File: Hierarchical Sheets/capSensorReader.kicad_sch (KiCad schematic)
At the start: 15 parts, among them U1 LM358, U2 LM358

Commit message: Redo Base Project file add code
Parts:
- removed V1, V2: 5, symbol Simulation_SPICE:VDC
- removed Vin1: VSIN, symbol Simulation_SPICE:VSIN
- C1: now left out of the parts list
- CSENSOR1: renamed from C2; now left out of the parts list
- Cf1, Cf2: footprint (none) -> Capacitor_THT:C_Disc_D3.8mm_W2.6mm_P2.50mm
- Ra1, Rb1, Rc1, Rd1, Rf1, Rf2: footprint (none) -> Resistor_THT:R_Axial_DIN0204_L3.6mm_D1.6mm_P5.08mm_Horizontal
- U2: footprint (none) -> Package_DIP:DIP-8_W7.62mm
- U2, U3: renamed from U1; footprint (none) -> Package_DIP:DIP-8_W7.62mm
- U3: renamed from U2; footprint (none) -> Package_DIP:DIP-8_W7.62mm
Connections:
- net V-: now reaches U2.4 (V-), U3.4 (V-)
- net Vsin: now reaches C1.1, CSENSOR1.1
- net V+: now reaches U2.8 (V+), U3.8 (V+)
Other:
- note removed: ".tran 10n 40u UIC"

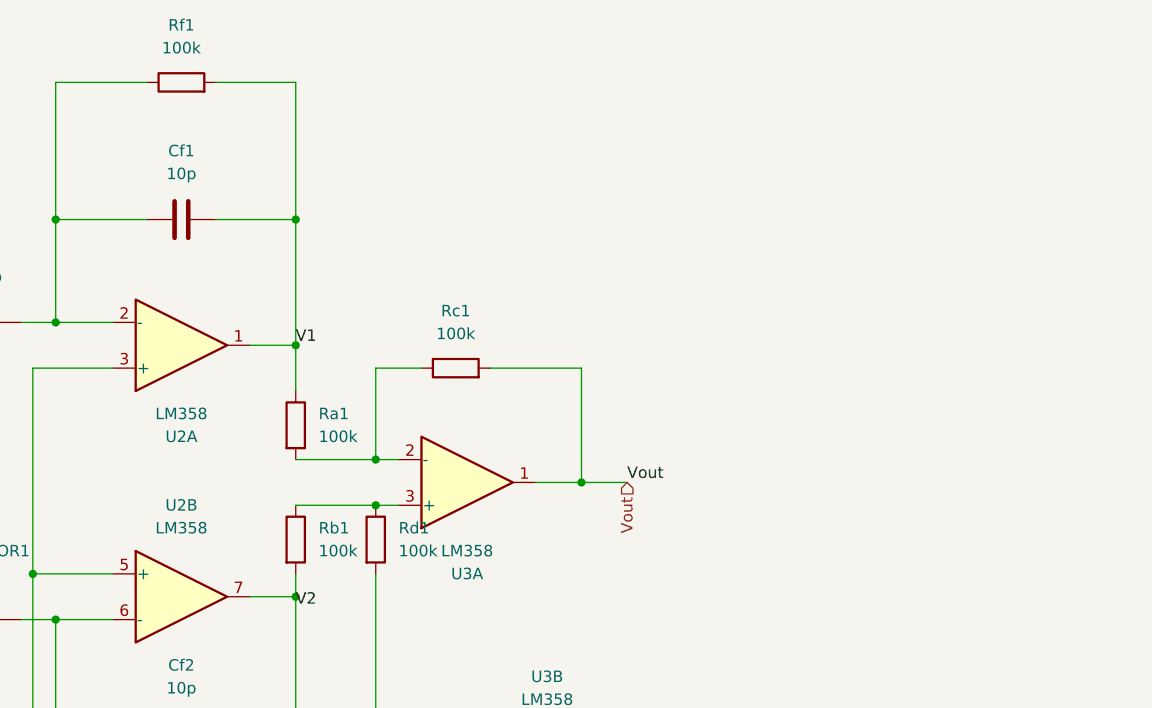
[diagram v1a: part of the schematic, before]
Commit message: Added rectifier and passive low-pass filter (RC)
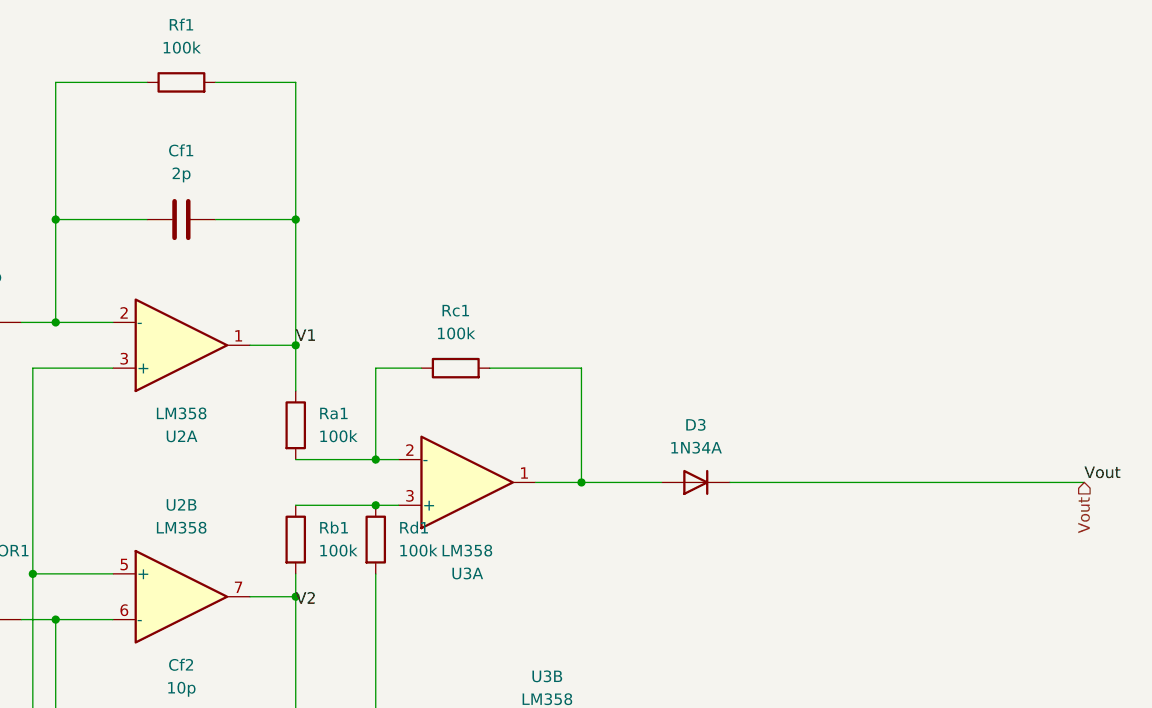
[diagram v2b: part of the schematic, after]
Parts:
- added D3: 1N34A, Diode_THT:D_DO-35_SOD27_P2.54mm_Vertical_AnodeUp, symbol Device:D
- Cf1: value 10p -> 2p
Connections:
- net Vout: now also D3.1 (K); no longer Rc1.2, U3.1
- new net: D3.2 (A), Rc1.2, U3.1
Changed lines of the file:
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@@
+	)
+	(junction
+		(at 114.3 59.69)
+		(diameter 0)
+		(color 0 0 0 0)
+	)
+	(junction
+		(at 111.76 99.06)
+		(diameter 0)
+		(color 0 0 0 0)
+	)
+	(junction
+		(at 149.86 91.44)
+		(diameter 0)
+		(color 0 0 0 0)
+	)
+	(junction
+		(at 140.97 101.6)
+		(diameter 0)
+		(color 0 0 0 0)
+	)
+	(junction
+		(at 114.3 104.14)
+		(diameter 0)
+		(color 0 0 0 0)
+	)
+	(junction
+		(at 140.97 59.69)
+		(diameter 0)
+		(color 0 0 0 0)
+	)
+	(junction
+		(at 114.3 71.12)
+		(diameter 0)
+		(color 0 0 0 0)
+	)
+	(junction
+		(at 140.97 116.84)
+		(diameter 0)
+		(color 0 0 0 0)
+	)
+	(junction
+		(at 66.04 100.33)
+		(diameter 0)
+		(color 0 0 0 0)
 	)
 	(junction
@@
 		(color 0 0 0 0)
 	)
-	(junction
-		(at 114.3 59.69)
-		(diameter 0)
-		(color 0 0 0 0)
-	)
-	(junction
-		(at 111.76 99.06)
-		(diameter 0)
-		(color 0 0 0 0)
-	)
-	(junction
-		(at 149.86 91.44)
-		(diameter 0)
-		(color 0 0 0 0)
-	)
-	(junction
-		(at 140.97 101.6)
-		(diameter 0)
-		(color 0 0 0 0)
-	)
-	(junction
-		(at 114.3 104.14)
-		(diameter 0)
-		(color 0 0 0 0)
-	)
-	(junction
-		(at 140.97 59.69)
-		(diameter 0)
-		(color 0 0 0 0)
-	)
-	(junction
-		(at 114.3 71.12)
-		(diameter 0)
-		(color 0 0 0 0)
-	)
-	(junction
-		(at 140.97 116.84)
-		(diameter 0)
-		(color 0 0 0 0)
-	)
-	(junction
-		(at 66.04 100.33)
-		(diameter 0)
-		(color 0 0 0 0)
-	)
 	(no_connect
 		(at 161.29 118.11)
@@
 	(wire
 		(pts
-			(xy 172.72 88.9) (xy 177.8 88.9)
-		)
-		(stroke
-			(width 0)
-			(type default)
-		)
-	)
-	(wire
-		(pts
 			(xy 135.89 73.66) (xy 140.97 73.66)
 		)
@@
 		(pts
 			(xy 132.08 44.45) (xy 140.97 44.45)
+		)
+		(stroke
+			(width 0)
+			(type default)
+		)
+	)
+	(wire
+		(pts
+			(xy 172.72 88.9) (xy 181.61 88.9)
+		)
+		(stroke
+			(width 0)
+			(type default)
+		)
+	)
+	(wire
+		(pts
+			(xy 189.23 88.9) (xy 228.6 88.9)
 		)
 		(stroke
@@
 	)
 	(label "Vout"
-		(at 177.8 88.9 0)
+		(at 228.6 88.9 0)
 		(effects
 			(font
@@
 	(hierarchical_label "Vout"
 		(shape input)
-		(at 177.8 88.9 270)
+		(at 228.6 88.9 270)
 		(effects
 			(font
@@
 			)
 		)
-		(property "Value" "10p"
+		(property "Value" "2p"
 			(at 128.27 54.61 90)
 			(effects
@@
 					(unit 1)
 				)
+			)
+		)
+	)
+	(symbol
+		(lib_id "Device:D")
+		(at 185.42 88.9 180)
+		(unit 1)
+		(exclude_from_sim no)
+		(in_bom yes)
+		(on_board yes)
+		(dnp no)
+		(fields_autoplaced yes)
+		(property "Reference" "D3"
+			(at 185.42 82.55 0)
+			(effects
+				(font
+					(size 1.27 1.27)
+				)
+			)
+		)
+		(property "Value" "1N34A"
+			(at 185.42 85.09 0)
+			(effects
+				(font
+					(size 1.27 1.27)
+				)
+			)
+		)
+		(property "Footprint" "Diode_THT:D_DO-35_SOD27_P2.54mm_Vertical_AnodeUp"
+			(at 185.42 88.9 0)
+			(effects
+				(font
+					(size 1.27 1.27)
+				)
+				(hide yes)
+			)
+		)
+		(property "Datasheet" "~"
+			(at 185.42 88.9 0)
+			(effects
+				(font
+					(size 1.27 1.27)
+				)
+				(hide yes)
+			)
+		)
+		(property "Description" "Diode"
+			(at 185.42 88.9 0)
+			(effects
+				(font
+					(size 1.27 1.27)
+				)
+				(hide yes)
+			)
+		)
+		(property "Sim.Library" ".\\"
+			(at 185.42 88.9 0)
+			(effects
+				(font
+					(size 1.27 1.27)
+				)
+				(hide yes)
+			)
+		)
+		(pin "1"
+		)
+		(pin "2"
+		)
+		(instances
+			(project ""
+				(path "/eb20fb8b-6e33-462b-9505-401dab49dd09/b20763cf-135f-4c80-a439-1f71268d237b"
+					(reference "D3")
+					(unit 1)
+				)
+				(path "/eb20fb8b-6e33-462b-9505-401dab49dd09/d1fc981b-0a3d-4bee-b8f0-81f28e3ff9d1"
+					(reference "D4")
+					(unit 1)
+				)

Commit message: Update Main Sub Sheets
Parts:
- removed Ra1, Rb1, Rd1: 100k, Resistor_THT:R_Axial_DIN0204_L3.6mm_D1.6mm_P5.08mm_Horizontal, symbol Device:R
- removed unit 1 of U3
- added C1, C13, C14: 100p, symbol Device:C
- added R11, Rc3, Rc5: 1k, symbol Device:R
- added R12: 500, symbol Device:R
- added Rc4: 100k, symbol Device:R
- added U3: INA128, symbol Amplifier_Instrumentation:INA128
- Rc1: footprint Resistor_THT:R_Axial_DIN0204_L3.6mm_D1.6mm_P5.08mm_Horizontal -> (none)
- renumbered C1 to C2, CSENSOR1 to CSENSOR2, Cf1 to Cf3, Cf2 to Cf4, Rf1 to Rf3, Rf2 to Rf4, U2 to U4, U3 to U5
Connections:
- net GND: now also C1.2, C13.2, C14.2, U3.5 (Ref)
- net V+: now also U3.7 (V+)
- net V-: now also U3.4 (V-)
- net V1: now also U3.3 (+)
- net V2: now also U3.2 (-)
- net Vout: now also U5.7, R11.2; no longer D3.1 (K)
- net at Rc1.1: now also D3.1 (K), C1.1
- net at Rc1.2: now also Rc3.2, Rc4.1; no longer D3.2 (A)
- net at U5.5 (+): now also Rc4.2, Rc5.2
- net at U5.6 (-): now also R11.1
- new net: C14.1, Rc5.1
- new net: R12.1, U3.1 (Rg)
- new net: D3.2 (A), U3.6
- new net: R12.2, U3.8 (Rg)
- new net: C13.1, Rc3.1
- no-connect marks 3 -> 0
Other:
- moved on the sheet: C2, CSENSOR2, Cf3, Cf4, Rf3, Rf4, U4A, U4B, U5B

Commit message: Main Update
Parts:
- C16: renamed from C1; footprint (none) -> Capacitor_THT:C_Disc_D3.8mm_W2.6mm_P2.50mm
- C17: renamed from C13; footprint (none) -> Capacitor_THT:C_Disc_D3.8mm_W2.6mm_P2.50mm
- C18: renamed from C14; footprint (none) -> Capacitor_THT:C_Disc_D3.8mm_W2.6mm_P2.50mm
- R13: renamed from R12; footprint (none) -> Resistor_THT:R_Axial_DIN0204_L3.6mm_D1.6mm_P5.08mm_Horizontal
- R14: renamed from R11; footprint (none) -> Resistor_THT:R_Axial_DIN0204_L3.6mm_D1.6mm_P5.08mm_Horizontal
- Rc2: renamed from Rc1; footprint (none) -> Resistor_THT:R_Axial_DIN0204_L3.6mm_D1.6mm_P5.08mm_Horizontal
- Rc6: renamed from Rc3; footprint (none) -> Resistor_THT:R_Axial_DIN0204_L3.6mm_D1.6mm_P5.08mm_Horizontal
- Rc7: renamed from Rc4; footprint (none) -> Resistor_THT:R_Axial_DIN0204_L3.6mm_D1.6mm_P5.08mm_Horizontal
- Rc8: renamed from Rc5; footprint (none) -> Resistor_THT:R_Axial_DIN0204_L3.6mm_D1.6mm_P5.08mm_Horizontal
- U13: renamed from U3; footprint (none) -> Package_DIP:DIP-8_W7.62mm
- renumbered C2 to C15, CSENSOR2 to CSENSOR1, Cf3 to Cf1, Cf4 to Cf2, D3 to D4, Rf3 to Rf1, Rf4 to Rf2, U5 to U12, U4 to U2

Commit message: PCB designed rev1.0
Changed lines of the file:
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@@
 		(dnp no)
 		(property "Reference" "U13"
-			(at 175.26 82.4798 0)
+			(at 166.116 82.804 0)
 			(effects
 				(font

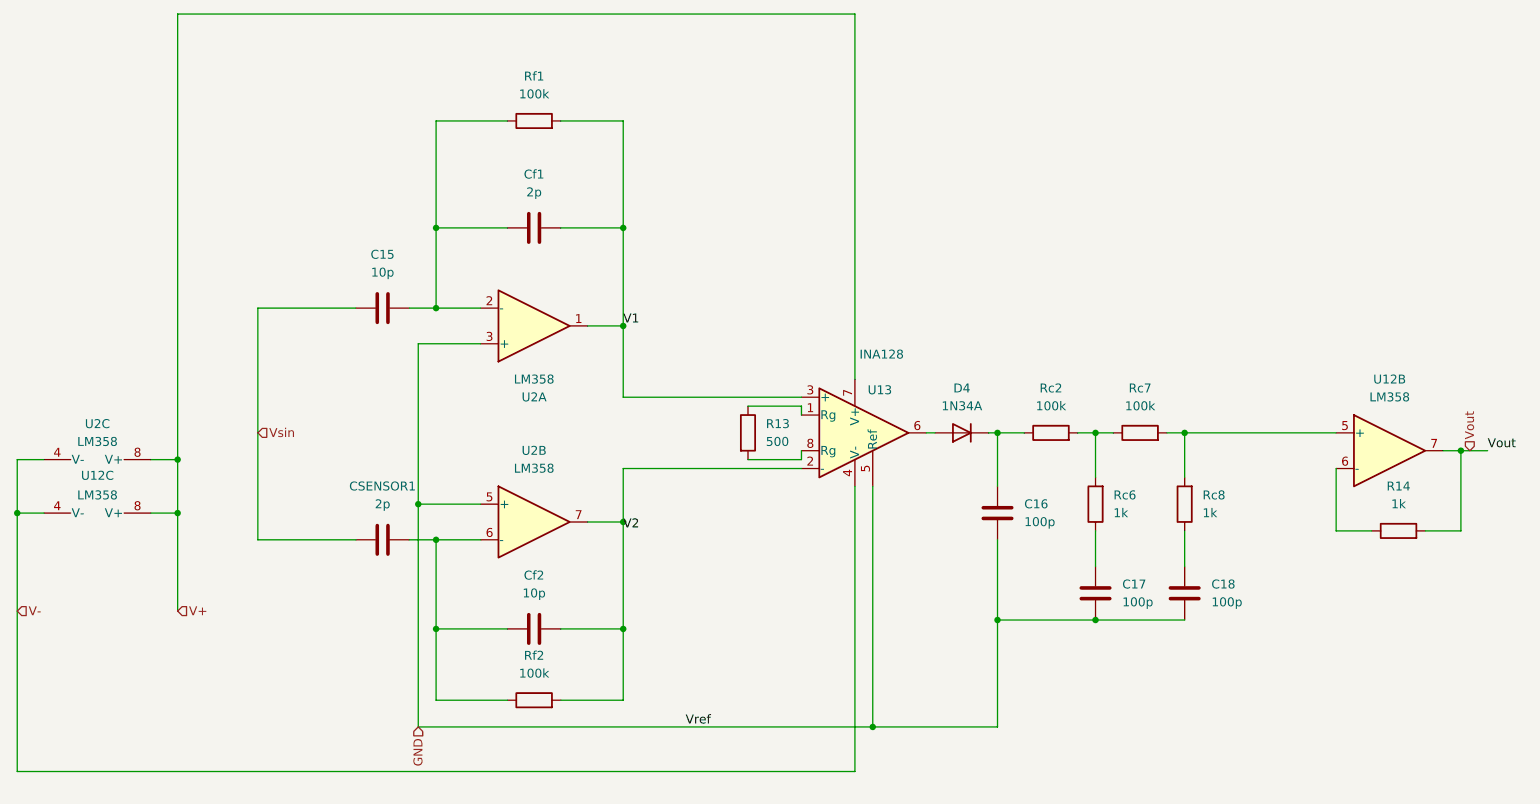
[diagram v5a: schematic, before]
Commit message: Remove extra ref sensor
each module had a reference sensor before, now have single ref sensor comparing to both sensors
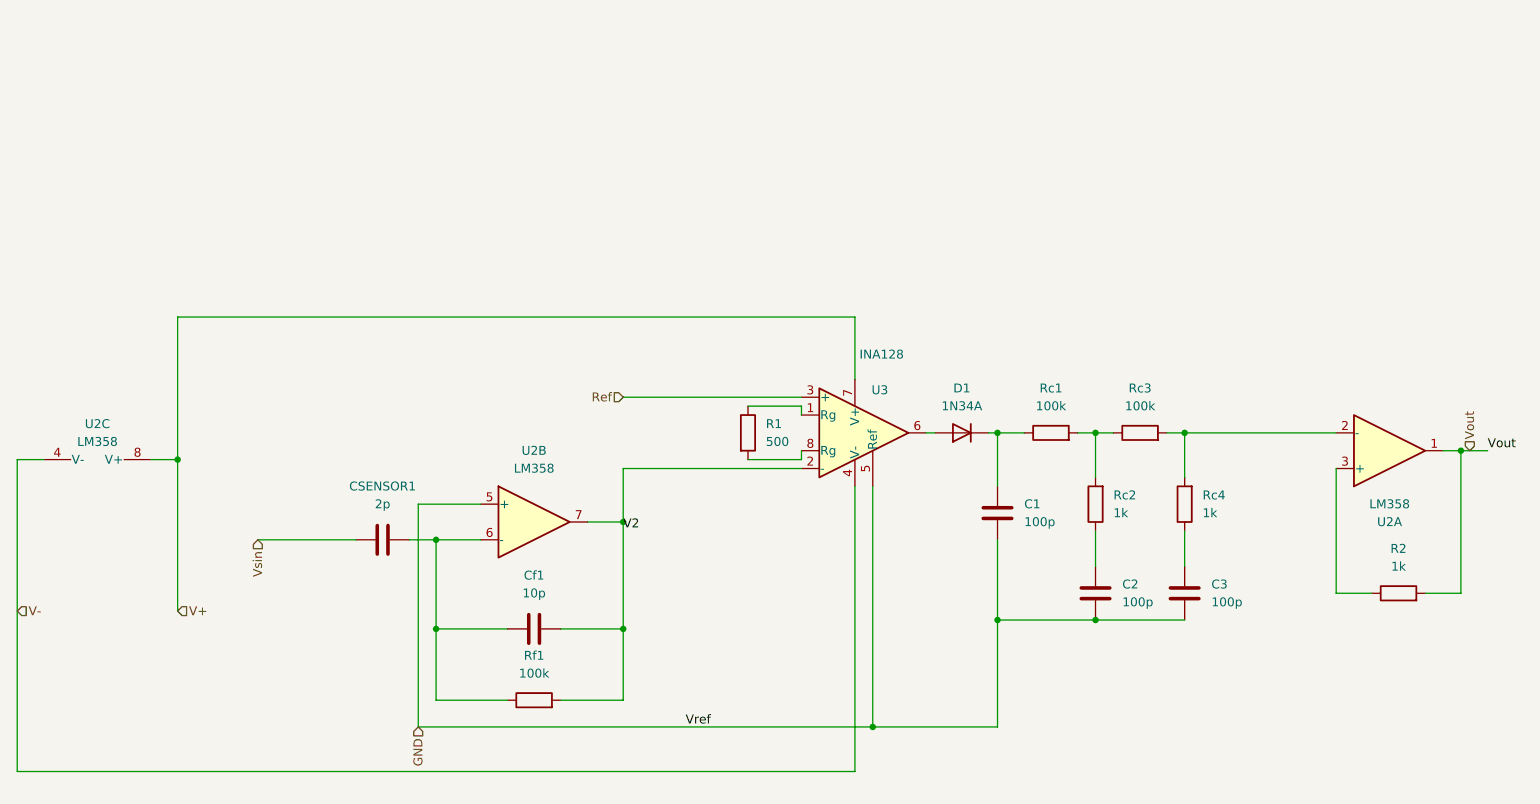
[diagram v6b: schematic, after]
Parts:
- removed C15: 10p, symbol Device:C
- removed Cf1: 2p, Capacitor_THT:C_Disc_D3.8mm_W2.6mm_P2.50mm, symbol Device:C
- removed Rf1: 100k, Resistor_THT:R_Axial_DIN0204_L3.6mm_D1.6mm_P5.08mm_Horizontal, symbol Device:R
- removed U12: LM358, Package_DIP:DIP-8_W7.62mm, symbol Amplifier_Operational:LM358
- renumbered C16 to C1, C17 to C2, C18 to C3, Cf2 to Cf1, D4 to D1, R13 to R1, R14 to R2, Rc2 to Rc1, Rc6 to Rc2, Rc7 to Rc3, Rc8 to Rc4, Rf2 to Rf1, U13 to U3
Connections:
- net GND: no longer U2.3 (+)
- net Vout: now also U2.1
- net at Rc3.2, Rc4.2: now also U2.2 (-)
- net at R2.1: now also U2.3 (+)
- net V1 renamed Ref
- net Ref: no longer U2.1
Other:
- moved on the sheet: R2

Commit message: Revert "Remove extra ref sensor"
This reverts commit 7f0b0207ac24b991faee57c630f393e10dd69dda.
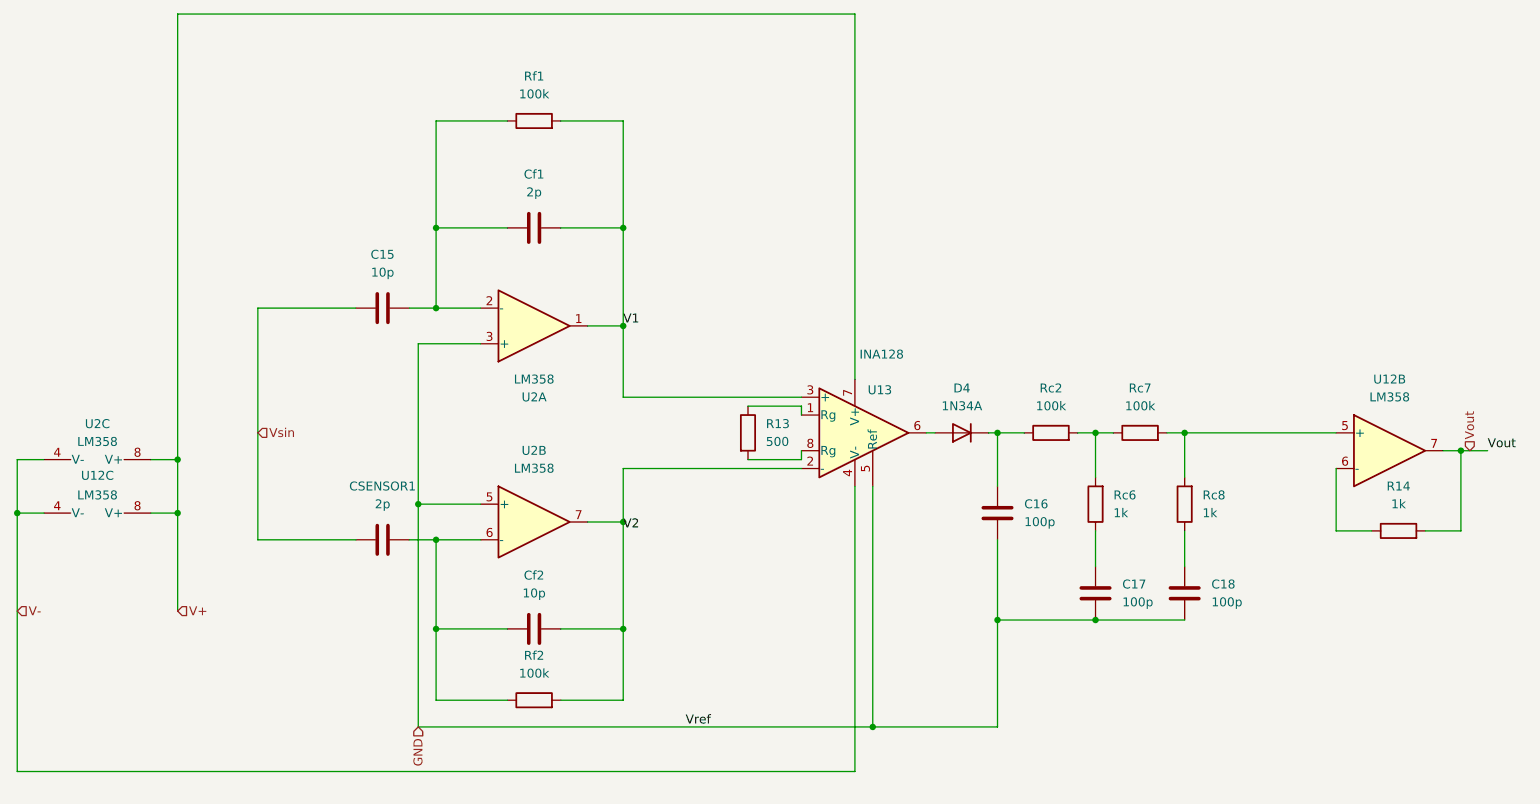
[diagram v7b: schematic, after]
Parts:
- added C15: 10p, symbol Device:C
- added Cf1: 2p, Capacitor_THT:C_Disc_D3.8mm_W2.6mm_P2.50mm, symbol Device:C
- added Rf1: 100k, Resistor_THT:R_Axial_DIN0204_L3.6mm_D1.6mm_P5.08mm_Horizontal, symbol Device:R
- added U12: LM358, Package_DIP:DIP-8_W7.62mm, symbol Amplifier_Operational:LM358
- renumbered C1 to C16, C2 to C17, C3 to C18, Cf1 to Cf2, D1 to D4, R1 to R13, R2 to R14, Rc1 to Rc2, Rc2 to Rc6, Rc3 to Rc7, Rc4 to Rc8, Rf1 to Rf2, U3 to U13
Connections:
- net GND: now also U2.3 (+)
- net V+: now also U12.8 (V+)
- net V-: now also U12.4 (V-)
- net Vout: now also U12.7; no longer U2.1
- net Vsin: now also C15.1
- net at Rc7.2, Rc8.2: now also U12.5 (+); no longer U2.2 (-)
- net at R14.1: now also U12.6 (-); no longer U2.3 (+)
- net Ref renamed V1
- net V1: now also U2.1, Cf1.2, Rf1.2
- new net: C15.2, Cf1.1, Rf1.1, U2.2 (-)
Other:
- moved on the sheet: R14
